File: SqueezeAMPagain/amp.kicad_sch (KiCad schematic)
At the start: 38 parts, among them U1 TAS5756M

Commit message: Update .gitignore, L_Radial_D12.0mm_P5+6+7.00mm_Fastron_11P.kicad_mod, SqueezeAMPagain.kicad_pcb, and 13 more files
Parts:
- removed C38: 2.2u/25V, Capacitor_SMD:C_0603_1608Metric, symbol Device:C
- removed JP1, JP2: SolderJumper_3_Bridged12, Jumper:SolderJumper-3_P1.3mm_Bridged12_RoundedPad1.0x1.5mm, symbol Jumper:SolderJumper_3_Bridged12
- added C59: 100n, Capacitor_SMD:C_0603_1608Metric, symbol Device:C
- added C60: 10u/50V, Capacitor_SMD:C_1206_3216Metric, symbol Device:C
- added C61, C62: 2.2u/25V, Capacitor_SMD:C_0805_2012Metric, symbol Device:C
- added C70, C72: 470u, Capacitor_THT:CP_Radial_D10.0mm_P5.00mm_P7.50mm, symbol Device:C_Polarized
- added JP1, JP2, JP6, JP7: Mono, Jumper:SolderJumper-2_P1.3mm_Open_RoundedPad1.0x1.5mm, symbol Jumper:SolderJumper_2_Open
- added R10, R11, R8, R9: 33, Resistor_SMD:R_0402_1005Metric, symbol Device:R
- added R21: 49.9k, Resistor_SMD:R_0603_1608Metric, symbol Device:R
- C1, C10, C11, C12, C14, C15, C16, C17, C18, C36: footprint Capacitor_SMD:C_0603_1608Metric -> Capacitor_SMD:C_0805_2012Metric
- C20, C21, C23, C25, C27: value 22u/35V -> 10u/50V
- C28, C29, C30, C31: footprint Capacitor_SMD:CP_Elec_6.3x3.9 -> Capacitor_THT:CP_Radial_D10.0mm_P5.00mm_P7.50mm; reichelt (none) -> FR-A 470U 35
- L5, L6, L7: value L -> 680nH; footprint Inductor_SMD:L_0603_1608Metric -> Inductor_SMD:L_0805_2012Metric; mfr (none) -> 0805F-R68K-08; reichelt (none) -> L-0805F 0,68µ
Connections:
- net GND: now also U1.20 (ADR1), U1.26 (ADR0), JP6.2 (B), JP7.2 (B), R21.2
- net GVDD_REG: now also C62.2
- net LRCLK/FS: now also R11.1; no longer U1.25 (LRCK/FS)
- net MCLK: now also R10.1; no longer U1.22 (MCLK)
- net PGND: now also C62.1, C70.2, C72.2
- net PVDD: now also C70.1, C72.1
- net SCLK: now also R9.1; no longer U1.23 (SCLK)
- net SDIN: now also R8.1; no longer U1.24 (SDIN)
- net SpeakerChannelA+/Amp_out: now also JP1.2 (B)
- net SpeakerChannelA-/Amp_out: now also JP1.1 (A)
- net SpeakerChannelB+/Amp_out: now also JP2.2 (B)
- net SpeakerChannelB-/Amp_out: now also JP2.1 (A)
- net at C11.1, U1.36 (DAC_OUTB): now also R21.1
- net at C11.2, U1.37 (SPK_INB+): now also JP7.1 (A)
- net at C12.1, U1.38 (SPK_INB-): now also JP6.1 (A)
- new net: R8.2, U1.24 (SDIN)
- new net: R10.2, U1.22 (MCLK)
- new net: R9.2, U1.23 (SCLK)
- new net: R11.2, U1.25 (LRCK/FS)
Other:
- title: (none) -> Amplifier section
- moved on the sheet: C36, R100, R101

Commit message: Update SqueezeAMPagain.kicad_pcb, SqueezeAMPagain.kicad_prl, USB-Uart.kicad_sch, and 4 more files
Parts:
- removed L5, L6, L7: 680nH, Inductor_SMD:L_0805_2012Metric, symbol Device:L
- removed R10, R11, R8, R9: 33, Resistor_SMD:R_0402_1005Metric, symbol Device:R
- added FB1, FB2, FB3, FB4: 600Ω@100MHz 500mA, Inductor_SMD:L_0805_2012Metric, symbol Device:FerriteBead_Small
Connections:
- net +3.3V: now also FB4.1
- net GND: now also FB2.1, FB3.1
- net GNDA: now also FB3.2
- net LRCLK/FS: now also U1.25 (LRCK/FS)
- net MCLK: now also U1.22 (MCLK)
- net PGND: now also FB2.2
- net SCLK: now also U1.23 (SCLK)
- net SDIN: now also U1.24 (SDIN)
- net at C18.1, C32.1, U1.14 (AVDD): now also FB4.2

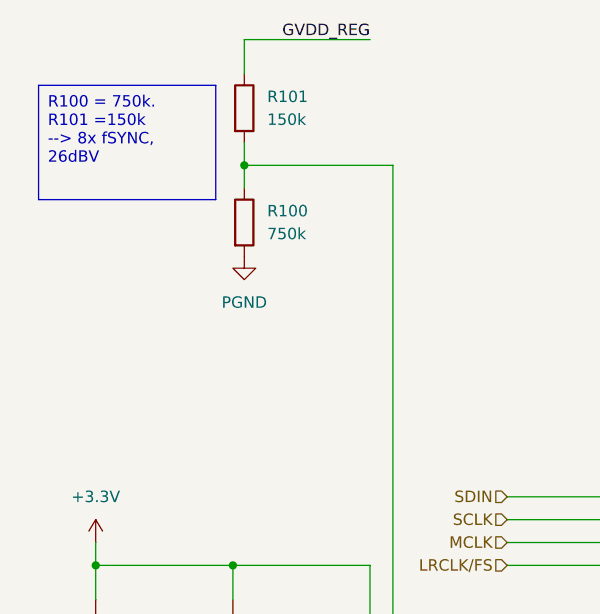
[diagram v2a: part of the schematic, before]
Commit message: Update SqueezeAMPagain.kicad_pcb, SqueezeAMPagain.kicad_sch, USB-Uart.kicad_sch, and 4 more files
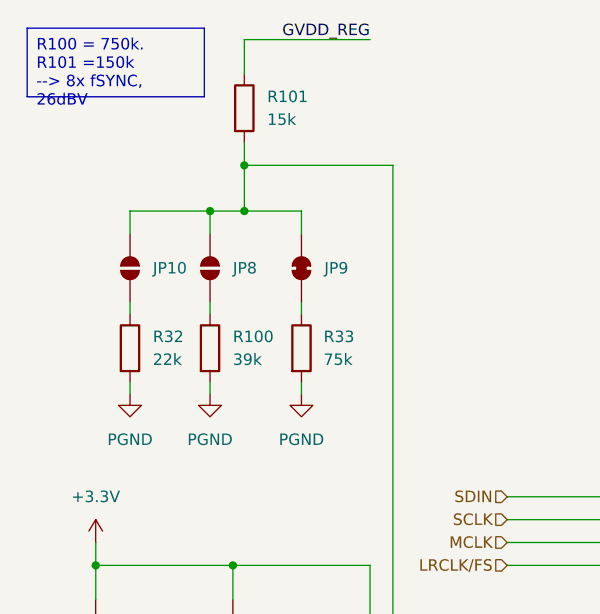
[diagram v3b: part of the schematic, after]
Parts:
- added JP10, JP8: SolderJumper_2_Open, Jumper:SolderJumper-2_P1.3mm_Open_RoundedPad1.0x1.5mm, symbol Jumper:SolderJumper_2_Open
- added JP9: SolderJumper_2_Bridged, Jumper:SolderJumper-2_P1.3mm_Bridged_RoundedPad1.0x1.5mm, symbol Jumper:SolderJumper_2_Bridged
- added R32: 22k, Resistor_SMD:R_0603_1608Metric, symbol Device:R
- added R33: 75k, Resistor_SMD:R_0603_1608Metric, symbol Device:R
- R100: value 750k -> 39k; JLCPCB (none) -> C23153
- R101: value 150k -> 15k; JLCPCB# (none) -> C22809
- R21: JLCPCB# (none) -> C23184
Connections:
- net PGND: now also R32.2, R33.2
- net at R101.2, U1.9 (SPK_GAIN/FREQ): now also JP10.2 (B), JP8.2 (B), JP9.2 (B); no longer R100.1
- new net: JP8.1 (A), R100.1
- new net: JP9.1 (A), R33.1
- new net: JP10.1 (A), R32.1
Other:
- moved on the sheet: R100

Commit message: Update SqueezeAMPagain.kicad_pcb, SqueezeAMPagain.kicad_pro, amp.kicad_sch, and 2 more files
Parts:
- removed C59: 100n, Capacitor_SMD:C_0603_1608Metric, symbol Device:C
- removed C60: 10u/50V, Capacitor_SMD:C_1206_3216Metric, symbol Device:C
- removed C61: 2.2u/25V, Capacitor_SMD:C_0805_2012Metric, symbol Device:C
- removed FB1, FB2: 600Ω@100MHz 500mA, Inductor_SMD:L_0805_2012Metric, symbol Device:FerriteBead_Small
- added JP11: Mono, Jumper:SolderJumper-2_P1.3mm_Open_RoundedPad1.0x1.5mm, symbol Jumper:SolderJumper_2_Open
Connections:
- net at C11.1, U1.36 (DAC_OUTB): now also JP11.1 (A); no longer R21.1
- new net: JP11.2 (B), R21.1

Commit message: Update L_Radial_D12.0mm_P5+6+7.00mm_Fastron_11P.kicad_mod, SqueezeAMPagain.kicad_pcb, SqueezeAMPagain.kicad_prl, and 5 more files
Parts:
- removed FB3: 600Ω@100MHz 500mA, Inductor_SMD:L_0805_2012Metric, symbol Device:FerriteBead_Small
- added C84: 10u/50V, Capacitor_SMD:C_1206_3216Metric, symbol Device:C
- added C85, C86, C87, C88: 100n, Capacitor_SMD:C_0603_1608Metric, symbol Device:C
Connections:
- net GND is gone; now on net PGND: C10.2, C12.2, C14.2, C16.2, C17.2, C33.2, C34.2, C35.2, C36.2, C37.2, JP6.2 (B), JP7.2 (B), R21.2, U1.20 (ADR1), U1.26 (ADR0), U1.29 (DGND), U1.33 (GND)
- net GNDA is gone; now on net PGND: C18.2, C32.2, U1.10 (AGND), U1.15 (AGND)
- net PGND: now also C84.2, C85.2, C86.2, C87.2, C88.2
- net PVDD: now also C84.1, C85.1, C86.1, C87.1, C88.1
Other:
- moved on the sheet: C20, C21, C23, C24, C25, C26, C27

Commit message: Update SqueezeAMPagain.kicad_pcb, SqueezeAMPagain.kicad_prl, SqueezeAMPagain.kicad_pro, and 11 more files
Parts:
- renumbered C16 to C1, C15 to C10, C70 to C11, C32 to C12, C28 to C13, C29 to C14, C30 to C15, C31 to C16, C21 to C17, C19 to C18, C72 to C19, C36 to C2, C1 to C20, C20 to C21, C13 to C22, C10 to C23, C85 to C24, C23 to C25, C86 to C26, C11 to C27, C26 to C28, C25 to C29, C33 to C3, C12 to C30, C24 to C31, C27 to C32, C87 to C33, C39 to C34, C84 to C35, C88 to C36, C62 to C37, C37 to C4, C14 to C5, C34 to C6, C17 to C7, C18 to C8, C35 to C9, FB4 to FB1, JP10 to JP1, JP8 to JP2, JP9 to JP3, JP1 to JP4, JP11 to JP5, JP2 to JP6, JP6 to JP8, R32 to R4, R100 to R5, R101 to R6, R33 to R7, R21 to R8

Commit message: Update SqueezeAMPagain.kicad_pcb, SqueezeAMPagain.kicad_prl, SqueezeAMPagain.kicad_pro, and 4 more files
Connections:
- net +3.3V: no longer C1.1, C2.1, C3.1, C4.1, C7.1, C9.1, U1.30 (DVDD), U1.31 (CPVDD), U1.35 (CPVSS)
- new net +3.3V_{SW}: C1.1, C2.1, C3.1, C4.1, C7.1, C9.1, U1.30 (DVDD), U1.31 (CPVDD), U1.35 (CPVSS)
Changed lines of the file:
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@@
 			)
 		)
-		(property "Value" "+3.3V"
-			(at 17.78 105.41 0)
+		(property "Value" "+3.3V_{SW}"
+			(at 20.32 109.2199 0)
 			(effects
 				(font
 					(size 1.27 1.27)
 				)
+				(justify left)
 			)
 		)
@@
 			)
 		)
-		(property "Value" "+3.3V"
-			(at 22.86 82.55 0)
+		(property "Value" "+3.3V_{SW}"
+			(at 25.4 86.3599 0)
 			(effects
 				(font
 					(size 1.27 1.27)
 				)
+				(justify left)
 			)
 		)
@@
 			)
 		)
-		(property "Value" "+3.3V"
+		(property "Value" "+3.3V_{SW}"
 			(at 79.502 117.856 0)
 			(effects
